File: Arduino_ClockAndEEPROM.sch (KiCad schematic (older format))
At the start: 0 parts

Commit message: Created new child sheet, added majority of the symbols.
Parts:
- added BT?: Battery, symbol Device:Battery
- added C? (x2): C, symbol Device:C
- added C?: CP, symbol Device:CP
- added D?: LED, symbol Device:LED
- added R? (x2): R, symbol Device:R
- added U?: 24LC1025, symbol Memory_EEPROM:24LC1025
- added U?: ATmega328P-AU, Package_QFP:TQFP-32_7x7mm_P0.8mm, symbol MCU_Microchip_ATmega:ATmega328P-AU
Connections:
- new net: U?.21 (GND), U?.3 (GND), U?.5 (GND)
- new net: U?.4 (VCC), U?.6 (VCC)
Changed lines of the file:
@@
 $Descr A4 11693 8268
 encoding utf-8
-Sheet 1 1
+Sheet 1 2
 Title "Arduino Clone w 512K EEPROM & Clock"
 Date "2019-06-05"
@@
 Comment4 ""
 $EndDescr
+$Comp
+L Device:Battery BT?
+U 1 1 5CF8CC53
+P 4400 2350
+F 0 "BT?" H 4508 2396 50  0000 L CNN
+F 1 "Battery" H 4508 2305 50  0000 L CNN
+F 2 "" V 4400 2410 50  0001 C CNN
+F 3 "~" V 4400 2410 50  0001 C CNN
+	1    4400 2350
+	1    0    0    -1
+$EndComp
+$Comp
+L Device:C C?
+U 1 1 5CF8DA61
+P 5750 1500
+F 0 "C?" H 5865 1546 50  0000 L CNN
+F 1 "C" H 5865 1455 50  0000 L CNN
+F 2 "" H 5788 1350 50  0001 C CNN
+F 3 "~" H 5750 1500 50  0001 C CNN
+	1    5750 1500
+	1    0    0    -1
+$EndComp
+$Comp
+L Device:C C?
+U 1 1 5CF8DFBA
+P 5750 2000
+F 0 "C?" H 5865 2046 50  0000 L CNN
+F 1 "C" H 5865 1955 50  0000 L CNN
+F 2 "" H 5788 1850 50  0001 C CNN
+F 3 "~" H 5750 2000 50  0001 C CNN
+	1    5750 2000
+	1    0    0    -1
+$EndComp
+$Comp
+L Device:CP C?
+U 1 1 5CF8E235
+P 5750 2750
+F 0 "C?" H 5868 2796 50  0000 L CNN
+F 1 "CP" H 5868 2705 50  0000 L CNN
+F 2 "" H 5788 2600 50  0001 C CNN
+F 3 "~" H 5750 2750 50  0001 C CNN
+	1    5750 2750
+	1    0    0    -1
+$EndComp
+$Comp
+L Device:LED D?
+U 1 1 5CF8E8D6
+P 5350 3150
+F 0 "D?" H 5343 3366 50  0000 C CNN
+F 1 "LED" H 5343 3275 50  0000 C CNN
+F 2 "" H 5350 3150 50  0001 C CNN
+F 3 "~" H 5350 3150 50  0001 C CNN
+	1    5350 3150
+	1    0    0    -1
+$EndComp
+$Comp
+L Device:R R?
+U 1 1 5CF8EF8E
+P 6850 1750
+F 0 "R?" H 6920 1796 50  0000 L CNN
+F 1 "R" H 6920 1705 50  0000 L CNN
+F 2 "" V 6780 1750 50  0001 C CNN
+F 3 "~" H 6850 1750 50  0001 C CNN
+	1    6850 1750
+	1    0    0    -1
+$EndComp
+$Comp
+L Device:R R?
+U 1 1 5CF8F355
+P 6850 2300
+F 0 "R?" H 6920 2346 50  0000 L CNN
+F 1 "R" H 6920 2255 50  0000 L CNN
+F 2 "" V 6780 2300 50  0001 C CNN
+F 3 "~" H 6850 2300 50  0001 C CNN
+	1    6850 2300
+	1    0    0    -1
+$EndComp
+$Comp
+L Memory_EEPROM:24LC1025 U?
+U 1 1 5CF8F7DF
+P 7700 2150
+F 0 "U?" H 7700 2631 50  0000 C CNN
+F 1 "24LC1025" H 7700 2540 50  0000 C CNN
+F 2 "" H 7700 2150 50  0001 C CNN
+F 3 "http://ww1.microchip.com/downloads/en/DeviceDoc/21941B.pdf" H 7700 2150 50  0001 C CNN
+	1    7700 2150
+	1    0    0    -1
+$EndComp
+$Comp
+L MCU_Microchip_ATmega:ATmega328P-AU U?
+U 1 1 5CF90E0E
+P 1950 2350
+F 0 "U?" H 1950 761 50  0000 C CNN
+F 1 "ATmega328P-AU" H 1950 670 50  0000 C CNN
+F 2 "Package_QFP:TQFP-32_7x7mm_P0.8mm" H 1950 2350 50  0001 C CIN
+F 3 "http://ww1.microchip.com/downloads/en/DeviceDoc/ATmega328_P%20AVR%20MCU%20with%20picoPower%20Technology%20Data%20Sheet%2040001984A.pdf" H 1950 2350 50  0001 C CNN
+	1    1950 2350
+	1    0    0    -1
+$EndComp
+$Sheet
+S 7300 3000 1000 1050
+U 5CF95995
+F0 "Connectors" 25
+F1 "Connector.sch" 25
+$EndSheet
 $EndSCHEMATC

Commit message: Added rest of the symbols.
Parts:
- added U?: DS1337_8pin_Bayterek, symbol Bayterek_Components:DS1337_8pin_Bayterek
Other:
- moved on the sheet: BT?, C?, D?, R?, U?
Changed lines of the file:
@@
 L Device:Battery BT?
 U 1 1 5CF8CC53
-P 4400 2350
-F 0 "BT?" H 4508 2396 50  0000 L CNN
-F 1 "Battery" H 4508 2305 50  0000 L CNN
-F 2 "" V 4400 2410 50  0001 C CNN
-F 3 "~" V 4400 2410 50  0001 C CNN
-	1    4400 2350
+P 1700 2050
+F 0 "BT?" H 1808 2096 50  0000 L CNN
+F 1 "Battery" H 1808 2005 50  0000 L CNN
+F 2 "" V 1700 2110 50  0001 C CNN
+F 3 "~" V 1700 2110 50  0001 C CNN
+	1    1700 2050
 	1    0    0    -1
 $EndComp
@@
 L Device:C C?
 U 1 1 5CF8DA61
-P 5750 1500
-F 0 "C?" H 5865 1546 50  0000 L CNN
-F 1 "C" H 5865 1455 50  0000 L CNN
-F 2 "" H 5788 1350 50  0001 C CNN
-F 3 "~" H 5750 1500 50  0001 C CNN
-	1    5750 1500
+P 2350 2050
+F 0 "C?" H 2465 2096 50  0000 L CNN
+F 1 "C" H 2465 2005 50  0000 L CNN
+F 2 "" H 2388 1900 50  0001 C CNN
+F 3 "~" H 2350 2050 50  0001 C CNN
+	1    2350 2050
 	1    0    0    -1
 $EndComp
@@
 L Device:C C?
 U 1 1 5CF8DFBA
-P 5750 2000
-F 0 "C?" H 5865 2046 50  0000 L CNN
-F 1 "C" H 5865 1955 50  0000 L CNN
-F 2 "" H 5788 1850 50  0001 C CNN
-F 3 "~" H 5750 2000 50  0001 C CNN
-	1    5750 2000
+P 2350 2550
+F 0 "C?" H 2465 2596 50  0000 L CNN
+F 1 "C" H 2465 2505 50  0000 L CNN
+F 2 "" H 2388 2400 50  0001 C CNN
+F 3 "~" H 2350 2550 50  0001 C CNN
+	1    2350 2550
 	1    0    0    -1
 $EndComp
@@
 L Device:CP C?
 U 1 1 5CF8E235
-P 5750 2750
-F 0 "C?" H 5868 2796 50  0000 L CNN
-F 1 "CP" H 5868 2705 50  0000 L CNN
-F 2 "" H 5788 2600 50  0001 C CNN
-F 3 "~" H 5750 2750 50  0001 C CNN
-	1    5750 2750
+P 2350 3000
+F 0 "C?" H 2468 3046 50  0000 L CNN
+F 1 "CP" H 2468 2955 50  0000 L CNN
+F 2 "" H 2388 2850 50  0001 C CNN
+F 3 "~" H 2350 3000 50  0001 C CNN
+	1    2350 3000
 	1    0    0    -1
 $EndComp
@@
 L Device:LED D?
 U 1 1 5CF8E8D6
-P 5350 3150
-F 0 "D?" H 5343 3366 50  0000 C CNN
-F 1 "LED" H 5343 3275 50  0000 C CNN
-F 2 "" H 5350 3150 50  0001 C CNN
-F 3 "~" H 5350 3150 50  0001 C CNN
-	1    5350 3150
+P 1700 2650
+F 0 "D?" H 1693 2866 50  0000 C CNN
+F 1 "LED" H 1693 2775 50  0000 C CNN
+F 2 "" H 1700 2650 50  0001 C CNN
+F 3 "~" H 1700 2650 50  0001 C CNN
+	1    1700 2650
 	1    0    0    -1
 $EndComp
@@
 L Device:R R?
 U 1 1 5CF8EF8E
-P 6850 1750
-F 0 "R?" H 6920 1796 50  0000 L CNN
-F 1 "R" H 6920 1705 50  0000 L CNN
-F 2 "" V 6780 1750 50  0001 C CNN
-F 3 "~" H 6850 1750 50  0001 C CNN
-	1    6850 1750
+P 2950 2000
+F 0 "R?" H 3020 2046 50  0000 L CNN
+F 1 "R" H 3020 1955 50  0000 L CNN
+F 2 "" V 2880 2000 50  0001 C CNN
+F 3 "~" H 2950 2000 50  0001 C CNN
+	1    2950 2000
 	1    0    0    -1
 $EndComp
@@
 L Device:R R?
 U 1 1 5CF8F355
-P 6850 2300
-F 0 "R?" H 6920 2346 50  0000 L CNN
-F 1 "R" H 6920 2255 50  0000 L CNN
-F 2 "" V 6780 2300 50  0001 C CNN
-F 3 "~" H 6850 2300 50  0001 C CNN
-	1    6850 2300
+P 2950 2550
+F 0 "R?" H 3020 2596 50  0000 L CNN
+F 1 "R" H 3020 2505 50  0000 L CNN
+F 2 "" V 2880 2550 50  0001 C CNN
+F 3 "~" H 2950 2550 50  0001 C CNN
+	1    2950 2550
 	1    0    0    -1
 $EndComp
@@
 L Memory_EEPROM:24LC1025 U?
 U 1 1 5CF8F7DF
-P 7700 2150
-F 0 "U?" H 7700 2631 50  0000 C CNN
-F 1 "24LC1025" H 7700 2540 50  0000 C CNN
-F 2 "" H 7700 2150 50  0001 C CNN
-F 3 "http://ww1.microchip.com/downloads/en/DeviceDoc/21941B.pdf" H 7700 2150 50  0001 C CNN
-	1    7700 2150
+P 7250 3500
+F 0 "U?" H 7250 3981 50  0000 C CNN
+F 1 "24LC1025" H 7250 3890 50  0000 C CNN
+F 2 "" H 7250 3500 50  0001 C CNN
+F 3 "http://ww1.microchip.com/downloads/en/DeviceDoc/21941B.pdf" H 7250 3500 50  0001 C CNN
+	1    7250 3500
 	1    0    0    -1
 $EndComp
@@
 L MCU_Microchip_ATmega:ATmega328P-AU U?
 U 1 1 5CF90E0E
-P 1950 2350
-F 0 "U?" H 1950 761 50  0000 C CNN
-F 1 "ATmega328P-AU" H 1950 670 50  0000 C CNN
-F 2 "Package_QFP:TQFP-32_7x7mm_P0.8mm" H 1950 2350 50  0001 C CIN
-F 3 "http://ww1.microchip.com/downloads/en/DeviceDoc/ATmega328_P%20AVR%20MCU%20with%20picoPower%20Technology%20Data%20Sheet%2040001984A.pdf" H 1950 2350 50  0001 C CNN
-	1    1950 2350
+P 5400 3900
+F 0 "U?" H 5400 2311 50  0000 C CNN
+F 1 "ATmega328P-AU" H 5400 2220 50  0000 C CNN
+F 2 "Package_QFP:TQFP-32_7x7mm_P0.8mm" H 5400 3900 50  0001 C CIN
+F 3 "http://ww1.microchip.com/downloads/en/DeviceDoc/ATmega328_P%20AVR%20MCU%20with%20picoPower%20Technology%20Data%20Sheet%2040001984A.pdf" H 5400 3900 50  0001 C CNN
+	1    5400 3900
 	1    0    0    -1
 $EndComp
 $Sheet
-S 7300 3000 1000 1050
+S 8900 4850 1000 1050
 U 5CF95995
 F0 "Connectors" 25
 F1 "Connector.sch" 25
 $EndSheet
+$Comp
+L Bayterek_Components:DS1337_8pin_Bayterek U?
+U 1 1 5CFA1F88
+P 7850 4400
+F 0 "U?" H 7250 4529 49  0000 C CNN
+F 1 "DS1337_8pin_Bayterek" H 7250 4439 49  0000 C CNN
+F 2 "" H 7900 4500 49  0001 C CNN
+F 3 "http://www.farnell.com/datasheets/2000844.pdf?_ga=2.2648176.1329014715.1559527073-834126407.1559527073" H 7900 4500 49  0001 C CNN
+	1    7850 4400
+	1    0    0    -1
+$EndComp
 $EndSCHEMATC

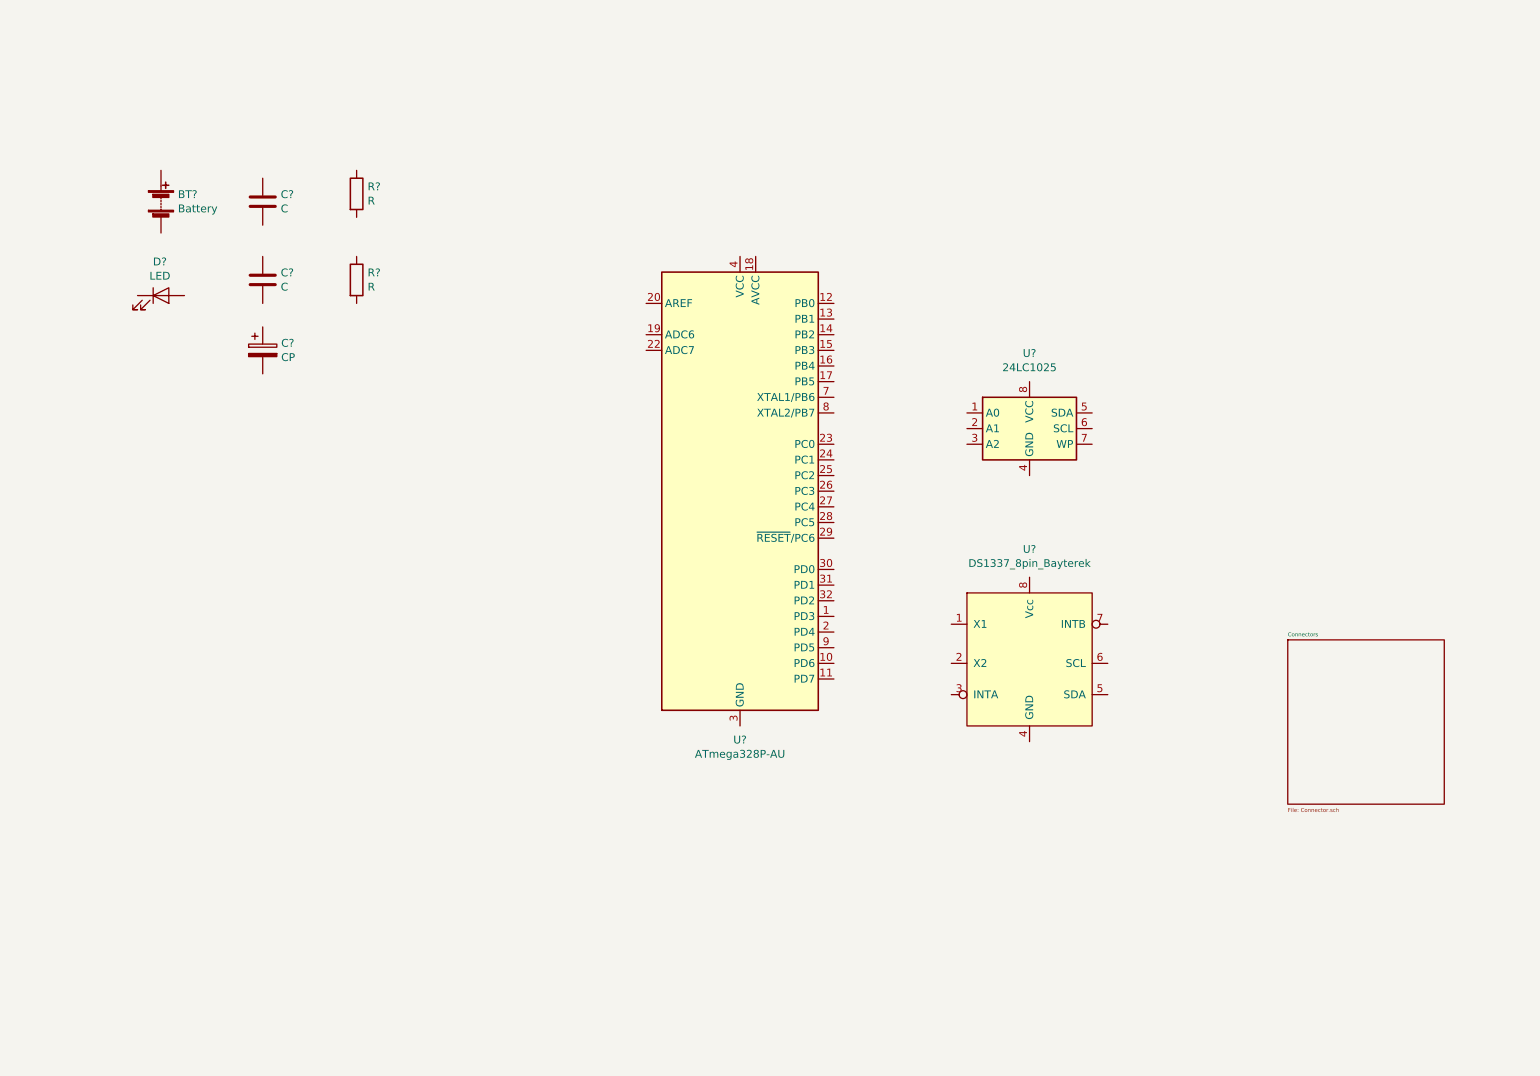
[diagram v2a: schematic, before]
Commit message: Added missing symbols, arranged symbols, annotated.
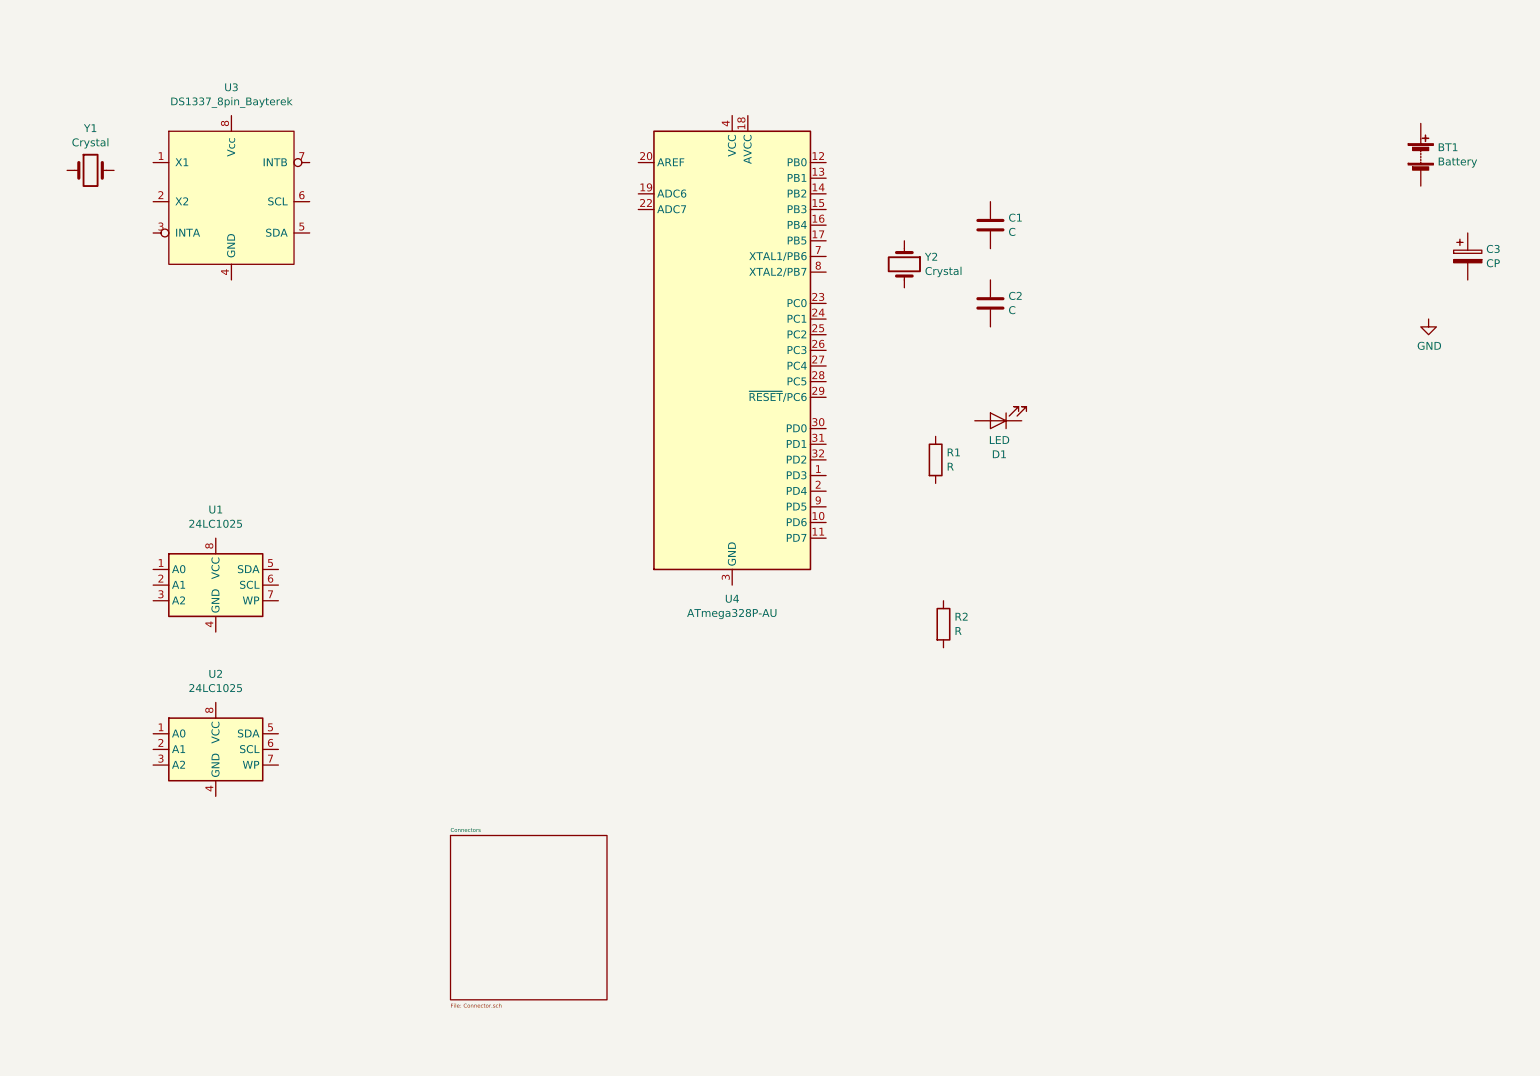
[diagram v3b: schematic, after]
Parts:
- added U2: 24LC1025, symbol Memory_EEPROM:24LC1025
- added Y1, Y2: Crystal, symbol Device:Crystal
- gave numbers to parts that had none: 10
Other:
- moved on the sheet: BT1, C1, C2, C3, D1, R1, R2, U1, U3, U4
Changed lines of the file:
@@
 $EndDescr
 $Comp
-L Device:Battery BT?
+L Device:Battery BT1
 U 1 1 5CF8CC53
-P 1700 2050
-F 0 "BT?" H 1808 2096 50  0000 L CNN
-F 1 "Battery" H 1808 2005 50  0000 L CNN
-F 2 "" V 1700 2110 50  0001 C CNN
-F 3 "~" V 1700 2110 50  0001 C CNN
-	1    1700 2050
+P 9750 1750
+F 0 "BT1" H 9858 1796 50  0000 L CNN
+F 1 "Battery" H 9858 1705 50  0000 L CNN
+F 2 "" V 9750 1810 50  0001 C CNN
+F 3 "~" V 9750 1810 50  0001 C CNN
+	1    9750 1750
 	1    0    0    -1
 $EndComp
 $Comp
-L Device:C C?
+L Device:C C1
 U 1 1 5CF8DA61
-P 2350 2050
-F 0 "C?" H 2465 2096 50  0000 L CNN
-F 1 "C" H 2465 2005 50  0000 L CNN
-F 2 "" H 2388 1900 50  0001 C CNN
-F 3 "~" H 2350 2050 50  0001 C CNN
-	1    2350 2050
+P 7000 2200
+F 0 "C1" H 7115 2246 50  0000 L CNN
+F 1 "C" H 7115 2155 50  0000 L CNN
+F 2 "" H 7038 2050 50  0001 C CNN
+F 3 "~" H 7000 2200 50  0001 C CNN
+	1    7000 2200
 	1    0    0    -1
 $EndComp
 $Comp
-L Device:C C?
+L Device:C C2
 U 1 1 5CF8DFBA
-P 2350 2550
-F 0 "C?" H 2465 2596 50  0000 L CNN
-F 1 "C" H 2465 2505 50  0000 L CNN
-F 2 "" H 2388 2400 50  0001 C CNN
-F 3 "~" H 2350 2550 50  0001 C CNN
-	1    2350 2550
+P 7000 2700
+F 0 "C2" H 7115 2746 50  0000 L CNN
+F 1 "C" H 7115 2655 50  0000 L CNN
+F 2 "" H 7038 2550 50  0001 C CNN
+F 3 "~" H 7000 2700 50  0001 C CNN
+	1    7000 2700
 	1    0    0    -1
 $EndComp
 $Comp
-L Device:CP C?
+L Device:CP C3
 U 1 1 5CF8E235
-P 2350 3000
-F 0 "C?" H 2468 3046 50  0000 L CNN
-F 1 "CP" H 2468 2955 50  0000 L CNN
-F 2 "" H 2388 2850 50  0001 C CNN
-F 3 "~" H 2350 3000 50  0001 C CNN
-	1    2350 3000
+P 10050 2400
+F 0 "C3" H 10168 2446 50  0000 L CNN
+F 1 "CP" H 10168 2355 50  0000 L CNN
+F 2 "" H 10088 2250 50  0001 C CNN
+F 3 "~" H 10050 2400 50  0001 C CNN
+	1    10050 2400
 	1    0    0    -1
 $EndComp
 $Comp
-L Device:LED D?
+L Device:LED D1
 U 1 1 5CF8E8D6
-P 1700 2650
-F 0 "D?" H 1693 2866 50  0000 C CNN
-F 1 "LED" H 1693 2775 50  0000 C CNN
-F 2 "" H 1700 2650 50  0001 C CNN
-F 3 "~" H 1700 2650 50  0001 C CNN
-	1    1700 2650
+P 7050 3450
+F 0 "D1" H 7043 3666 50  0000 C CNN
+F 1 "LED" H 7043 3575 50  0000 C CNN
+F 2 "" H 7050 3450 50  0001 C CNN
+F 3 "~" H 7050 3450 50  0001 C CNN
+	1    7050 3450
+	-1   0    0    1
+$EndComp
+$Comp
+L Device:R R1
+U 1 1 5CF8EF8E
+P 6650 3700
+F 0 "R1" H 6720 3746 50  0000 L CNN
+F 1 "R" H 6720 3655 50  0000 L CNN
+F 2 "" V 6580 3700 50  0001 C CNN
+F 3 "~" H 6650 3700 50  0001 C CNN
+	1    6650 3700
 	1    0    0    -1
 $EndComp
 $Comp
-L Device:R R?
-U 1 1 5CF8EF8E
-P 2950 2000
-F 0 "R?" H 3020 2046 50  0000 L CNN
-F 1 "R" H 3020 1955 50  0000 L CNN
-F 2 "" V 2880 2000 50  0001 C CNN
-F 3 "~" H 2950 2000 50  0001 C CNN
-	1    2950 2000
+L Device:R R2
+U 1 1 5CF8F355
+P 6700 4750
+F 0 "R2" H 6770 4796 50  0000 L CNN
+F 1 "R" H 6770 4705 50  0000 L CNN
+F 2 "" V 6630 4750 50  0001 C CNN
+F 3 "~" H 6700 4750 50  0001 C CNN
+	1    6700 4750
 	1    0    0    -1
 $EndComp
 $Comp
-L Device:R R?
-U 1 1 5CF8F355
-P 2950 2550
-F 0 "R?" H 3020 2596 50  0000 L CNN
-F 1 "R" H 3020 2505 50  0000 L CNN
-F 2 "" V 2880 2550 50  0001 C CNN
-F 3 "~" H 2950 2550 50  0001 C CNN
-	1    2950 2550
+L Memory_EEPROM:24LC1025 U1
+U 1 1 5CF8F7DF
+P 2050 4500
+F 0 "U1" H 2050 4981 50  0000 C CNN
+F 1 "24LC1025" H 2050 4890 50  0000 C CNN
+F 2 "" H 2050 4500 50  0001 C CNN
+F 3 "http://ww1.microchip.com/downloads/en/DeviceDoc/21941B.pdf" H 2050 4500 50  0001 C CNN
+	1    2050 4500
 	1    0    0    -1
 $EndComp
 $Comp
-L Memory_EEPROM:24LC1025 U?
-U 1 1 5CF8F7DF
-P 7250 3500
-F 0 "U?" H 7250 3981 50  0000 C CNN
-F 1 "24LC1025" H 7250 3890 50  0000 C CNN
-F 2 "" H 7250 3500 50  0001 C CNN
-F 3 "http://ww1.microchip.com/downloads/en/DeviceDoc/21941B.pdf" H 7250 3500 50  0001 C CNN
-	1    7250 3500
-	1    0    0    -1
-$EndComp
-$Comp
-L MCU_Microchip_ATmega:ATmega328P-AU U?
+L MCU_Microchip_ATmega:ATmega328P-AU U4
 U 1 1 5CF90E0E
-P 5400 3900
-F 0 "U?" H 5400 2311 50  0000 C CNN
-F 1 "ATmega328P-AU" H 5400 2220 50  0000 C CNN
-F 2 "Package_QFP:TQFP-32_7x7mm_P0.8mm" H 5400 3900 50  0001 C CIN
-F 3 "http://ww1.microchip.com/downloads/en/DeviceDoc/ATmega328_P%20AVR%20MCU%20with%20picoPower%20Technology%20Data%20Sheet%2040001984A.pdf" H 5400 3900 50  0001 C CNN
-	1    5400 3900
+P 5350 3000
+F 0 "U4" H 5350 1411 50  0000 C CNN
+F 1 "ATmega328P-AU" H 5350 1320 50  0000 C CNN
+F 2 "Package_QFP:TQFP-32_7x7mm_P0.8mm" H 5350 3000 50  0001 C CIN
+F 3 "http://ww1.microchip.com/downloads/en/DeviceDoc/ATmega328_P%20AVR%20MCU%20with%20picoPower%20Technology%20Data%20Sheet%2040001984A.pdf" H 5350 3000 50  0001 C CNN
+	1    5350 3000
 	1    0    0    -1
 $EndComp
 $Sheet
-S 8900 4850 1000 1050
+S 3550 6100 1000 1050
 U 5CF95995
 F0 "Connectors" 25
@@
 $EndSheet
 $Comp
-L Bayterek_Components:DS1337_8pin_Bayterek U?
+L Bayterek_Components:DS1337_8pin_Bayterek U3
 U 1 1 5CFA1F88
-P 7850 4400
-F 0 "U?" H 7250 4529 49  0000 C CNN
-F 1 "DS1337_8pin_Bayterek" H 7250 4439 49  0000 C CNN
-F 2 "" H 7900 4500 49  0001 C CNN
-F 3 "http://www.farnell.com/datasheets/2000844.pdf?_ga=2.2648176.1329014715.1559527073-834126407.1559527073" H 7900 4500 49  0001 C CNN
-	1    7850 4400
+P 2750 1450
+F 0 "U3" H 2150 1579 49  0000 C CNN
+F 1 "DS1337_8pin_Bayterek" H 2150 1489 49  0000 C CNN
+F 2 "" H 2800 1550 49  0001 C CNN
+F 3 "http://www.farnell.com/datasheets/2000844.pdf?_ga=2.2648176.1329014715.1559527073-834126407.1559527073" H 2800 1550 49  0001 C CNN
+	1    2750 1450
 	1    0    0    -1
 $EndComp
+$Comp
+L Device:Crystal Y2
+U 1 1 5CFA2A28
+P 6450 2450
+F 0 "Y2" V 6404 2581 50  0000 L CNN
+F 1 "Crystal" V 6495 2581 50  0000 L CNN
+F 2 "" H 6450 2450 50  0001 C CNN
+F 3 "~" H 6450 2450 50  0001 C CNN
+	1    6450 2450
+	0    1    1    0
+$EndComp
+$Comp
+L Device:Crystal Y1
+U 1 1 5CFA2EB9
+P 1250 1850
+F 0 "Y1" H 1250 2118 50  0000 C CNN
+F 1 "Crystal" H 1250 2027 50  0000 C CNN
+F 2 "" H 1250 1850 50  0001 C CNN
+F 3 "~" H 1250 1850 50  0001 C CNN
+	1    1250 1850
+	1    0    0    -1
+$EndComp
+$Comp
+L Memory_EEPROM:24LC1025 U2
+U 1 1 5CFA87FE
+P 2050 5550
+F 0 "U2" H 2050 6031 50  0000 C CNN
+F 1 "24LC1025" H 2050 5940 50  0000 C CNN
+F 2 "" H 2050 5550 50  0001 C CNN
+F 3 "http://ww1.microchip.com/downloads/en/DeviceDoc/21941B.pdf" H 2050 5550 50  0001 C CNN
+	1    2050 5550
+	1    0    0    -1
+$EndComp
+$Comp
+L power:GND #PWR01
+U 1 1 5CFB0CCC
+P 9800 2800
+F 0 "#PWR01" H 9800 2550 50  0001 C CNN
+F 1 "GND" H 9805 2627 50  0000 C CNN
+F 2 "" H 9800 2800 50  0001 C CNN
+F 3 "" H 9800 2800 50  0001 C CNN
+	1    9800 2800
+	1    0    0    -1
+$EndComp
